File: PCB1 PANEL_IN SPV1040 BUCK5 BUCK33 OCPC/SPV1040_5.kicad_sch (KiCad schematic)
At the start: 14 parts, among them J2 SOLAR, U2 SPV1040TTR

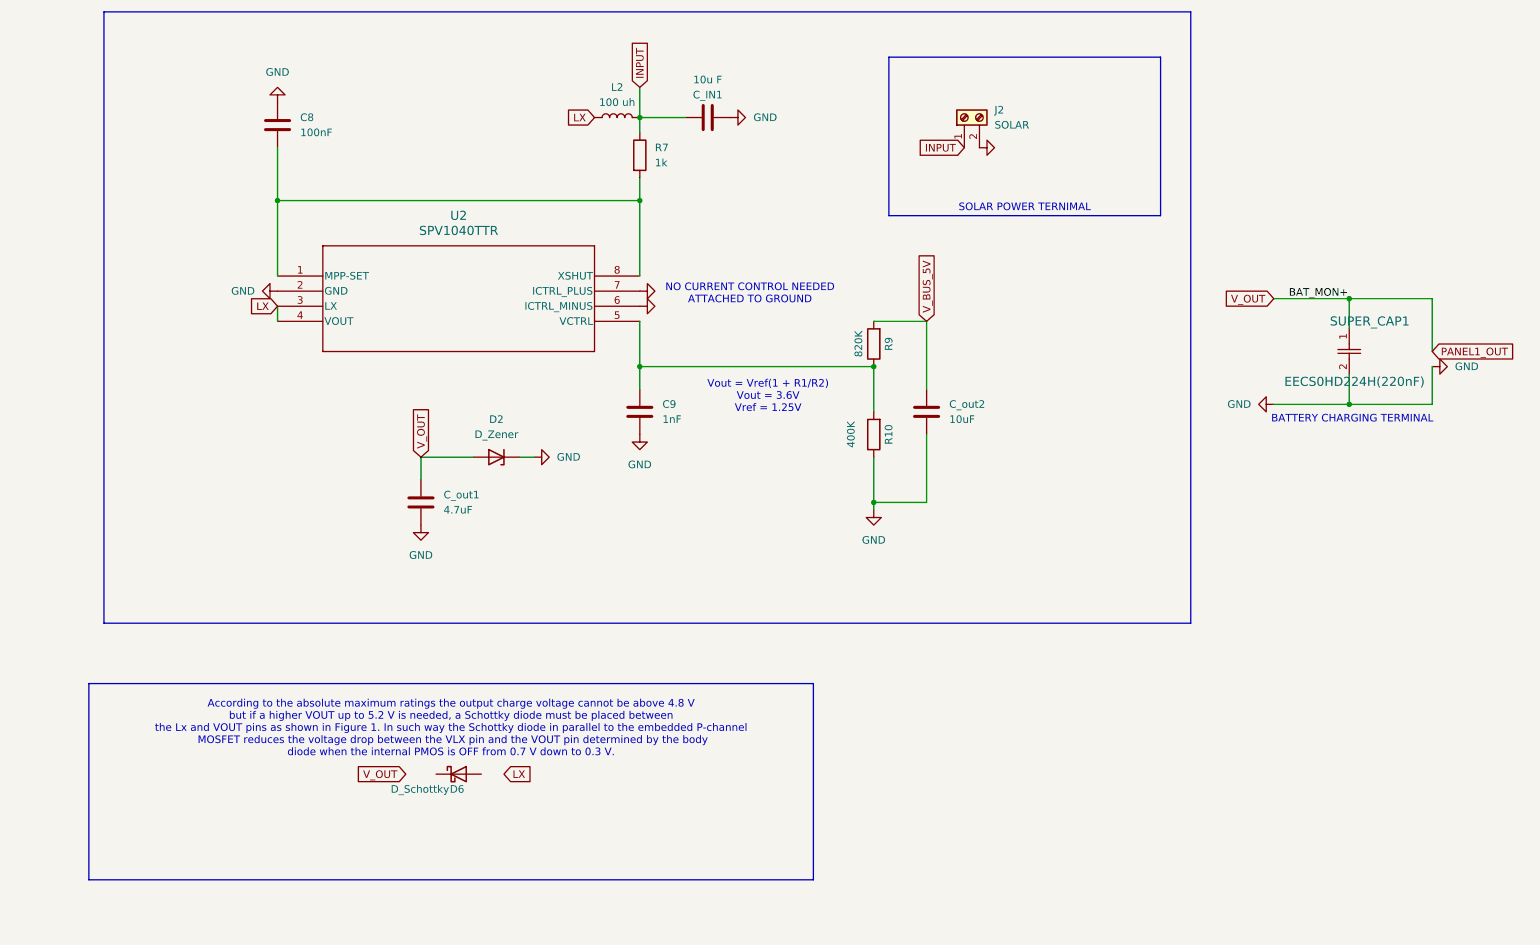
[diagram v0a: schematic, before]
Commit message: Changes
Added bucks from old work
and copied SPV
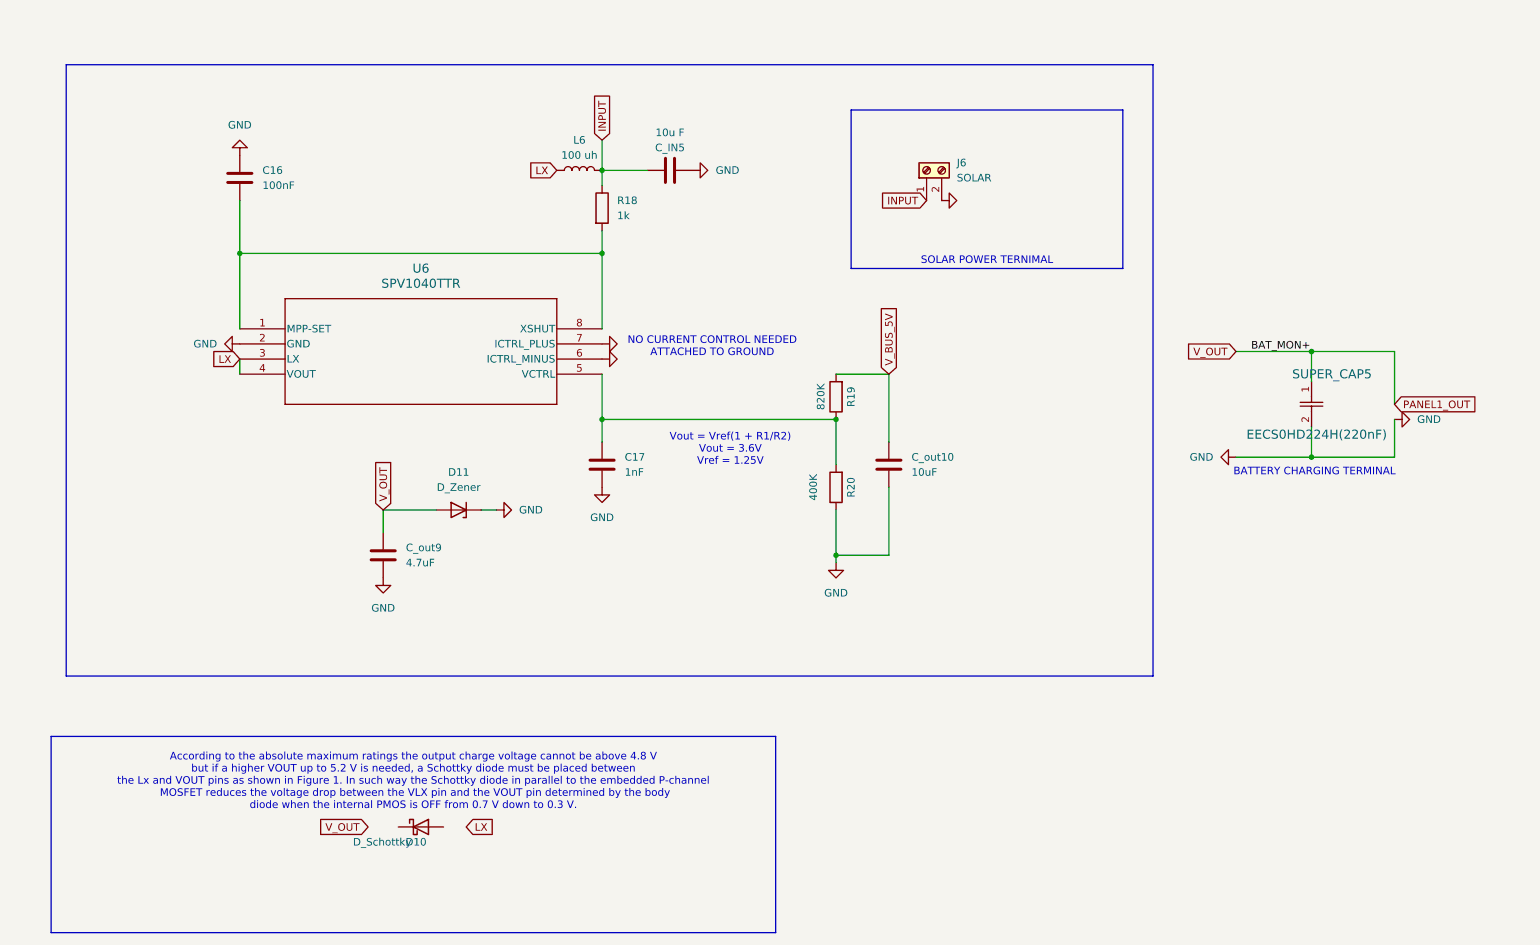
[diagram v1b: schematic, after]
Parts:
- removed C8: 100nF, Capacitor_SMD:C_0603_1608Metric, symbol Device:C
- removed C9: 1nF, Capacitor_SMD:C_0603_1608Metric, symbol Device:C
- removed C_IN1: 10u F, Capacitor_SMD:C_0603_1608Metric, symbol Device:C
- removed C_out1: 4.7uF, Capacitor_SMD:C_0603_1608Metric, symbol Device:C
- removed C_out2: 10uF, Capacitor_SMD:C_0603_1608Metric, symbol Device:C
- removed D2: D_Zener, Diode_SMD:D_1210_3225Metric, symbol Device:D_Zener
- removed D6: D_Schottky, symbol Device:D_Schottky
- removed J2: SOLAR, TerminalBlock_Phoenix:TerminalBlock_Phoenix_PT-1,5-2-5.0-H_1x02_P5.00mm_Horizontal, symbol Connector:Screw_Terminal_01x02
- removed L2: 100 uh, Inductor_SMD:L_Coilcraft_XAL6060-XXX, symbol Device:L
- removed R10: 400K, Resistor_SMD:R_0603_1608Metric, symbol Device:R
- removed R7: 1k, Resistor_SMD:R_0603_1608Metric, symbol Device:R
- removed R9: 820K, Resistor_SMD:R_0603_1608Metric, symbol Device:R
- removed SUPER_CAP1: EECS0HD224H(220nF), SPV1040T:CAP_EECS0_H_PAN, symbol 2024-06-08_06-57-05:super_capacitor
- removed U2: SPV1040TTR, SPV1040:SOP65P640X120-8N, symbol 2024-06-07_14-27-39:SPV1040TTR
- added C16: 100nF, Capacitor_SMD:C_0603_1608Metric, symbol Device:C
- added C17: 1nF, Capacitor_SMD:C_0603_1608Metric, symbol Device:C
- added C_IN5: 10u F, Capacitor_SMD:C_0603_1608Metric, symbol Device:C
- added C_out10: 10uF, Capacitor_SMD:C_0603_1608Metric, symbol Device:C
- added C_out9: 4.7uF, Capacitor_SMD:C_0603_1608Metric, symbol Device:C
- added D10: D_Schottky, symbol Device:D_Schottky
- added D11: D_Zener, Diode_SMD:D_1210_3225Metric, symbol Device:D_Zener
- added J6: SOLAR, TerminalBlock_Phoenix:TerminalBlock_Phoenix_PT-1,5-2-5.0-H_1x02_P5.00mm_Horizontal, symbol Connector:Screw_Terminal_01x02
- added L6: 100 uh, Inductor_SMD:L_Coilcraft_XAL6060-XXX, symbol Device:L
- added R18: 1k, Resistor_SMD:R_0603_1608Metric, symbol Device:R
- added R19: 820K, Resistor_SMD:R_0603_1608Metric, symbol Device:R
- added R20: 400K, Resistor_SMD:R_0603_1608Metric, symbol Device:R
- added SUPER_CAP5: EECS0HD224H(220nF), SPV1040T:CAP_EECS0_H_PAN, symbol 2024-06-08_06-57-05:super_capacitor
- added U6: SPV1040TTR, SPV1040:SOP65P640X120-8N, symbol 2024-06-07_14-27-39:SPV1040TTR
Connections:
- net GND: now also C16.1, C17.2, C_IN5.2, C_out10.2, C_out9.1, D11.1 (K), J6.2 (Pin_2), R20.1, SUPER_CAP5.2, U6.2 (GND), U6.6 (ICTRL_MINUS), U6.7 (ICTRL_PLUS)
- net INPUT: now also C_IN5.1, J6.1 (Pin_1), L6.2, R18.1
- net LX: now also L6.1, U6.3 (LX), U6.4 (VOUT)
- net PANEL1_OUT: now also C_out9.2, D11.2 (A), SUPER_CAP5.1
- net V_BUS_5V: now also C_out10.1, R19.2
- new net: C17.1, R19.1, R20.2, U6.5 (VCTRL)
- new net: C16.2, R18.2, U6.1 (MPP-SET), U6.8 (XSHUT)
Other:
- company: TEAM ANANT -> (none)
- title: SOLAR CHARGER -> (none)

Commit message: .
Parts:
- removed D11: D_Zener, Diode_SMD:D_1210_3225Metric, symbol Device:D_Zener
- added D: SMM4F5.0A-TR, CR_F5.0A-TR_STM, symbol 2025-01-24_10-07-25:SMM4F5.0A-TR
- C16: JLC Part  (none) -> C1525
- C17: JLC Part  (none) -> C1588
- C_IN5, C_out10: JLC Part  (none) -> C76614
- C_out9: JLC Part  (none) -> C69335
- L6: JLC Part  (none) -> C2911576
- R18: JLC Part  (none) -> C21190
- R19: JLC Part  (none) -> C2930044
- R20: JLC Part  (none) -> C3949569
- SUPER_CAP5: JLC Part  (none) -> C9900154460
- U6: JLC Part  (none) -> C221500
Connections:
- net GND: now also D.1
- net PANEL1_OUT: now also D.2

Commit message: Relabeling according to standards
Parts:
- D1801: renamed from D; footprint CR_F5.0A-TR_STM -> (none)
- renumbered C16 to C1801, C_IN5 to C1802, C_out9 to C1803, C_out10 to C1804, C17 to C1805, D10 to D1802, J6 to J1801, L6 to L1801, R18 to R1801, R19 to R1802, R20 to R1803, SUPER_CAP5 to SUPER_CAP1801, U6 to U1801
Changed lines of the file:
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@@
 		(dnp no)
 		(fields_autoplaced yes)
-		(property "Reference" "C_out10"
+		(property "Reference" "C1804"
 			(at 171.45 95.2499 0)
 			(effects
@@
 			(project "PCB1 PANEL_IN SPV1040 BUCK5 BUCK33 OCPC"
 				(path "/494c9d9f-6b33-4248-a813-27ffaaa929bd/8c378675-f65a-4b67-963a-3f9cd3fefa7d"
-					(reference "C_out10")
+					(reference "C1804")
 					(unit 1)
 				)
@@
 		(dnp no)
 		(fields_autoplaced yes)
-		(property "Reference" "C_out9"
+		(property "Reference" "C1803"
 			(at 86.36 110.4899 0)
 			(effects
@@
 			(project "PCB1 PANEL_IN SPV1040 BUCK5 BUCK33 OCPC"
 				(path "/494c9d9f-6b33-4248-a813-27ffaaa929bd/8c378675-f65a-4b67-963a-3f9cd3fefa7d"
-					(reference "C_out9")
+					(reference "C1803")
 					(unit 1)
 				)
@@
 		(dnp no)
 		(fields_autoplaced yes)
-		(property "Reference" "J6"
+		(property "Reference" "J1801"
 			(at 179.07 45.7199 90)
 			(effects
@@
 			(project "PCB1 PANEL_IN SPV1040 BUCK5 BUCK33 OCPC"
 				(path "/494c9d9f-6b33-4248-a813-27ffaaa929bd/8c378675-f65a-4b67-963a-3f9cd3fefa7d"
-					(reference "J6")
+					(reference "J1801")
 					(unit 1)
 				)
@@
 		(on_board yes)
 		(dnp no)
-		(property "Reference" "R20"
+		(property "Reference" "R1803"
 			(at 161.29 100.33 90)
 			(effects
@@
 			(project "PCB1 PANEL_IN SPV1040 BUCK5 BUCK33 OCPC"
 				(path "/494c9d9f-6b33-4248-a813-27ffaaa929bd/8c378675-f65a-4b67-963a-3f9cd3fefa7d"
-					(reference "R20")
+					(reference "R1803")
 					(unit 1)
 				)
@@
 		(on_board yes)
 		(dnp no)
-		(property "Reference" "D10"
-			(at 89.8526 160.02 0)
+		(property "Reference" "D1802"
+			(at 95.25 160.274 0)
 			(effects
 				(font
@@
 			(project "PCB1 PANEL_IN SPV1040 BUCK5 BUCK33 OCPC"
 				(path "/494c9d9f-6b33-4248-a813-27ffaaa929bd/8c378675-f65a-4b67-963a-3f9cd3fefa7d"
-					(reference "D10")
+					(reference "D1802")
 					(unit 1)
 				)
@@
 		(dnp no)
 		(fields_autoplaced yes)
-		(property "Reference" "U6"
+		(property "Reference" "U1801"
 			(at 88.9 63.5 0)
 			(effects
@@
 			(project "PCB1 PANEL_IN SPV1040 BUCK5 BUCK33 OCPC"
 				(path "/494c9d9f-6b33-4248-a813-27ffaaa929bd/8c378675-f65a-4b67-963a-3f9cd3fefa7d"
-					(reference "U6")
+					(reference "U1801")
 					(unit 1)
 				)
@@
 		(on_board yes)
 		(dnp no)
-		(property "Reference" "C_IN5"
+		(property "Reference" "C1802"
 			(at 130.81 43.18 90)
 			(effects
@@
 			(project "PCB1 PANEL_IN SPV1040 BUCK5 BUCK33 OCPC"
 				(path "/494c9d9f-6b33-4248-a813-27ffaaa929bd/8c378675-f65a-4b67-963a-3f9cd3fefa7d"
-					(reference "C_IN5")
+					(reference "C1802")
 					(unit 1)
 				)
@@
 		(dnp no)
 		(fields_autoplaced yes)
-		(property "Reference" "C16"
+		(property "Reference" "C1801"
 			(at 62.23 46.9899 0)
 			(effects
@@
 			(project "PCB1 PANEL_IN SPV1040 BUCK5 BUCK33 OCPC"
 				(path "/494c9d9f-6b33-4248-a813-27ffaaa929bd/8c378675-f65a-4b67-963a-3f9cd3fefa7d"
-					(reference "C16")
+					(reference "C1801")
 					(unit 1)
 				)
@@
 		(on_board yes)
 		(dnp no)
-		(property "Reference" "SUPER_CAP5"
+		(property "Reference" "SUPER_CAP1801"
 			(at 248.92 81.28 90)
 			(effects
@@
 			(project "PCB1 PANEL_IN SPV1040 BUCK5 BUCK33 OCPC"
 				(path "/494c9d9f-6b33-4248-a813-27ffaaa929bd/8c378675-f65a-4b67-963a-3f9cd3fefa7d"
-					(reference "SUPER_CAP5")
+					(reference "SUPER_CAP1801")
 					(unit 1)
 				)
@@
 		(on_board yes)
 		(dnp no)
-		(property "Reference" "R19"
+		(property "Reference" "R1802"
 			(at 161.29 85.09 90)
 			(effects
@@
 			(project "PCB1 PANEL_IN SPV1040 BUCK5 BUCK33 OCPC"
 				(path "/494c9d9f-6b33-4248-a813-27ffaaa929bd/8c378675-f65a-4b67-963a-3f9cd3fefa7d"
-					(reference "R19")
+					(reference "R1802")
 					(unit 1)
 				)
@@
 		(dnp no)
 		(fields_autoplaced yes)
-		(property "Reference" "C17"
+		(property "Reference" "C1805"
 			(at 123.19 95.2499 0)
 			(effects
@@
 			(project "PCB1 PANEL_IN SPV1040 BUCK5 BUCK33 OCPC"
 				(path "/494c9d9f-6b33-4248-a813-27ffaaa929bd/8c378675-f65a-4b67-963a-3f9cd3fefa7d"
-					(reference "C17")
+					(reference "C1805")
 					(unit 1)
 				)
@@
 		(dnp no)
 		(fields_autoplaced yes)
-		(property "Reference" "R18"
+		(property "Reference" "R1801"
 			(at 121.92 52.0699 0)
 			(effects
@@
 			(project "PCB1 PANEL_IN SPV1040 BUCK5 BUCK33 OCPC"
 				(path "/494c9d9f-6b33-4248-a813-27ffaaa929bd/8c378675-f65a-4b67-963a-3f9cd3fefa7d"
-					(reference "R18")
+					(reference "R1801")
 					(unit 1)
 				)
@@
 		(dnp no)
 		(fields_autoplaced yes)
-		(property "Reference" "L6"
+		(property "Reference" "L1801"
 			(at 115.57 41.91 90)
 			(effects
@@
 			(project "PCB1 PANEL_IN SPV1040 BUCK5 BUCK33 OCPC"
 				(path "/494c9d9f-6b33-4248-a813-27ffaaa929bd/8c378675-f65a-4b67-963a-3f9cd3fefa7d"
-					(reference "L6")
+					(reference "L1801")
 					(unit 1)
 				)
@@
 		(dnp no)
 		(fields_autoplaced yes)
-		(property "Reference" "D"
+		(property "Reference" "D1801"
 			(at 96.52 97.79 0)
 			(effects
@@
 			)
 		)
-		(property "Footprint" "CR_F5.0A-TR_STM"
+		(property "Footprint" ""
 			(at 91.44 104.14 0)
 			(effects
@@
 		(instances
 			(project ""
-				(path "/e98ca604-2429-4c57-b4a1-3d03a5ec156e"
+				(path "/494c9d9f-6b33-4248-a813-27ffaaa929bd/8c378675-f65a-4b67-963a-3f9cd3fefa7d"
+					(reference "D1801")
+					(unit 1)
+				)
+			)
+			(project ""
+				(path "/e98ca604-2429-4c57-b4a1-3d03a5ec156e"
